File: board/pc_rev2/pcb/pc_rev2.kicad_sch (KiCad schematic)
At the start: 17 parts, among them J1 Conn_01x24, J2 Conn_01x24, J3 GND Pins, J4 Conn_Grove_Host, J5 Conn_Grove-Analog_Host, J6 Conn_Grove-Analog_Host, J7 Conn_01x05, U1 Tang_nano_9K, U2 AE-FT234X

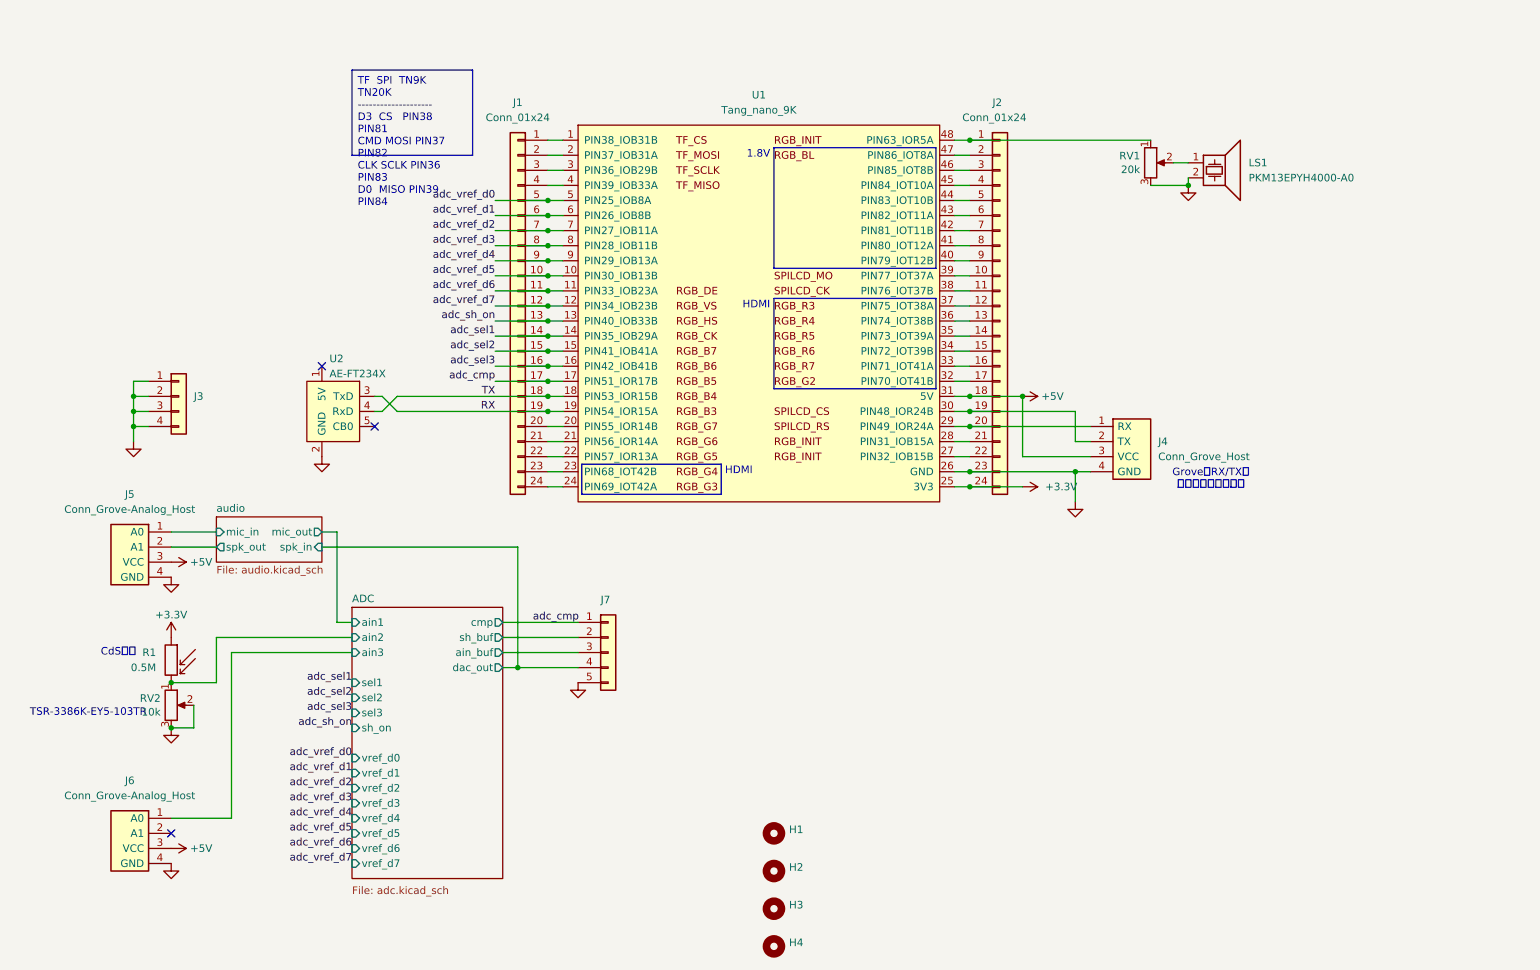
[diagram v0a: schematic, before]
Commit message: MSMP-IFを追加、スピーカ出力をOFFにする仕組みを追加（WIP）
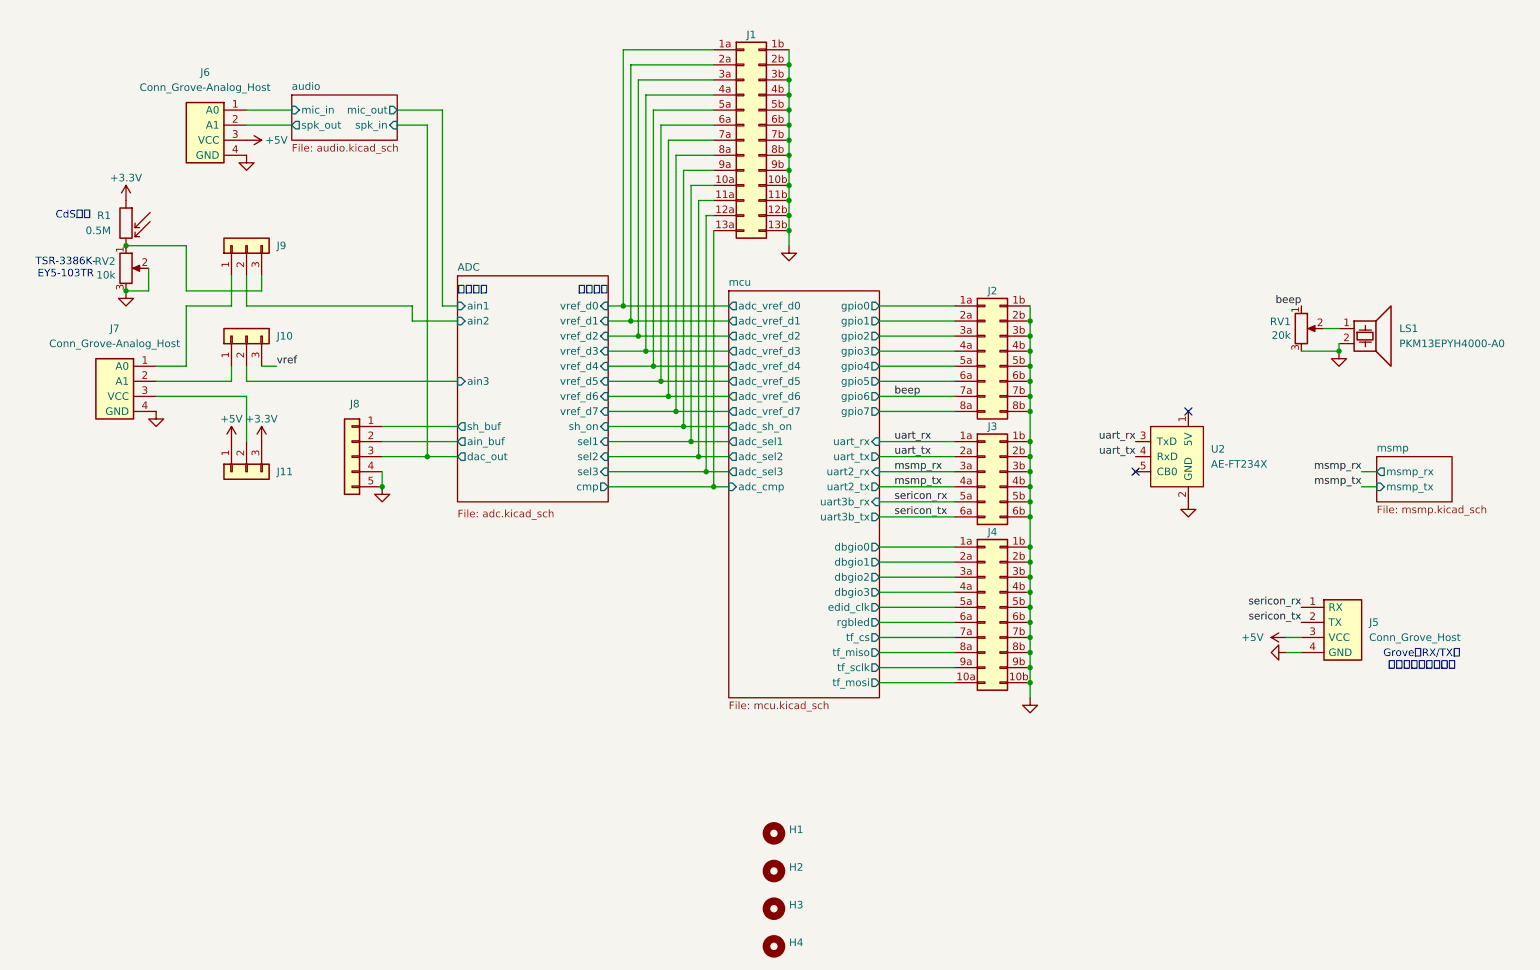
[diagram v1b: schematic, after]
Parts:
- removed J1, J2: Conn_01x24, Connector_PinHeader_2.54mm:PinHeader_1x24_P2.54mm_Vertical, symbol Connector_Generic:Conn_01x24
- removed J3: GND Pins, Connector_PinHeader_2.54mm:PinHeader_1x04_P2.54mm_Vertical, symbol Connector_Generic:Conn_01x04
- removed U1: Tang_nano_9K, uchan:DIP-48_Tang-Nano-9K, symbol uchan:Tang_nano_9K
- added J1: Conn_02x13_Odd_Even, symbol Connector_Generic:Conn_02x13_Row_Letter_Last
- added J10, J11, J9: Conn_01x03, Connector_PinHeader_2.54mm:PinHeader_1x03_P2.54mm_Vertical, symbol Connector_Generic:Conn_01x03
- added J2: Conn_02x08_Row_Letter_Last, symbol Connector_Generic:Conn_02x08_Row_Letter_Last
- added J3: Conn_02x06_Row_Letter_Last, symbol Connector_Generic:Conn_02x06_Row_Letter_Last
- added J4: Conn_02x10_Row_Letter_Last, symbol Connector_Generic:Conn_02x10_Row_Letter_Last
- renumbered J4 to J5, J5 to J6, J6 to J7, J7 to J8
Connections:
- net adc_cmp is gone; now on net ADC/sh_buf: J8.1 (Pin_1)
- net +3.3V: now also J11.3 (Pin_3)
- net +5V: now also J11.1 (Pin_1); no longer J7.3 (VCC)
- net ADC/ain2: now also J9.2 (Pin_2); no longer R1.2, RV2.1
- net ADC/ain3: now also J10.2 (Pin_2); no longer J7.1 (A0)
- net ADC/ain_buf: now also J8.2 (Pin_2); no longer J8.3 (Pin_3)
- net ADC/dac_out: now also J8.3 (Pin_3); no longer J8.4 (Pin_4)
- net ADC/sh_buf: no longer J8.2 (Pin_2)
- net GND: now also J8.4 (Pin_4), J1.10b (Pin_10b), J1.11b (Pin_11b), J1.12b (Pin_12b), J1.13b (Pin_13b), J1.1b (Pin_1b), J1.2b (Pin_2b), J1.3b (Pin_3b), J1.4b (Pin_4b), J1.5b (Pin_5b), J1.6b (Pin_6b), J1.7b (Pin_7b), J1.8b (Pin_8b), J1.9b (Pin_9b), J2.1b (Pin_1b), J2.2b (Pin_2b), J2.3b (Pin_3b), J2.4b (Pin_4b), J2.5b (Pin_5b), J2.6b (Pin_6b), J2.7b (Pin_7b), J2.8b (Pin_8b), J3.1b (Pin_1b), J3.2b (Pin_2b), J3.3b (Pin_3b), J3.4b (Pin_4b), J3.5b (Pin_5b), J3.6b (Pin_6b), J4.10b (Pin_10b), J4.1b (Pin_1b), J4.2b (Pin_2b), J4.3b (Pin_3b), J4.4b (Pin_4b), J4.5b (Pin_5b), J4.6b (Pin_6b), J4.7b (Pin_7b), J4.8b (Pin_8b), J4.9b (Pin_9b)
- net beep: now reaches RV1.1
- net beep: now also J2.7a (Pin_7a)
- net sericon_rx: now reaches J5.1 (RX)
- net sericon_rx: now also J3.5a (Pin_5a)
- net sericon_tx: now reaches J5.2 (TX)
- net sericon_tx: now also J3.6a (Pin_6a)
- net at J7.2 (A1): now also J10.1 (Pin_1)
- net RX renamed uart_rx
- net uart_rx: now also J3.1a (Pin_1a)
- net TX renamed uart_tx
- net uart_tx: now also J3.2a (Pin_2a)
- new net: J9.3 (Pin_3), R1.2, RV2.1
- new net: J11.2 (Pin_2), J7.3 (VCC)
- new net: J7.1 (A0), J9.1 (Pin_1)
- new net ADC/cmp: J1.13a (Pin_13a)
- new net ADC/sel1: J1.10a (Pin_10a)
- new net ADC/sel2: J1.11a (Pin_11a)
- new net ADC/sel3: J1.12a (Pin_12a)
- new net ADC/sh_on: J1.9a (Pin_9a)
- new net ADC/vref_d0: J1.1a (Pin_1a)
- new net ADC/vref_d1: J1.2a (Pin_2a)
- new net ADC/vref_d2: J1.3a (Pin_3a)
- new net ADC/vref_d3: J1.4a (Pin_4a)
- new net ADC/vref_d4: J1.5a (Pin_5a)
- new net ADC/vref_d5: J1.6a (Pin_6a)
- new net ADC/vref_d6: J1.7a (Pin_7a)
- new net ADC/vref_d7: J1.8a (Pin_8a)
- new net mcu/dbgio0: J4.1a (Pin_1a)
- new net mcu/dbgio1: J4.2a (Pin_2a)
- new net mcu/dbgio2: J4.3a (Pin_3a)
- new net mcu/dbgio3: J4.4a (Pin_4a)
- new net mcu/edid_clk: J4.5a (Pin_5a)
- new net mcu/gpio0: J2.1a (Pin_1a)
- new net mcu/gpio1: J2.2a (Pin_2a)
- new net mcu/gpio2: J2.3a (Pin_3a)
- new net mcu/gpio3: J2.4a (Pin_4a)
- new net mcu/gpio4: J2.5a (Pin_5a)
- new net mcu/gpio5: J2.6a (Pin_6a)
- new net mcu/gpio7: J2.8a (Pin_8a)
- new net mcu/rgbled: J4.6a (Pin_6a)
- new net mcu/tf_cs: J4.7a (Pin_7a)
- new net mcu/tf_miso: J4.8a (Pin_8a)
- new net mcu/tf_mosi: J4.10a (Pin_10a)
- new net mcu/tf_sclk: J4.9a (Pin_9a)
- new net msmp_rx: J3.3a (Pin_3a)
- new net msmp_tx: J3.4a (Pin_4a)
- new net vref: J10.3 (Pin_3)
- no-connect marks 3 -> 2
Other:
- added sheet mcu (mcu.kicad_sch)
- added sheet msmp (msmp.kicad_sch)
- note added: "TSR-3386K- EY5-103TR"
- note added: "アナログ"
- note added: "デジタル"
- note removed: "1.8V"
- note removed: "HDMI"
- note removed: "TSR-3386K-EY5-103TR"
- moved on the sheet: J5, J6, J7, J8, LS1, R1, RV1, RV2, U2

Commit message: ADCの8ch化＆スピーカーミュートの仕組み変更
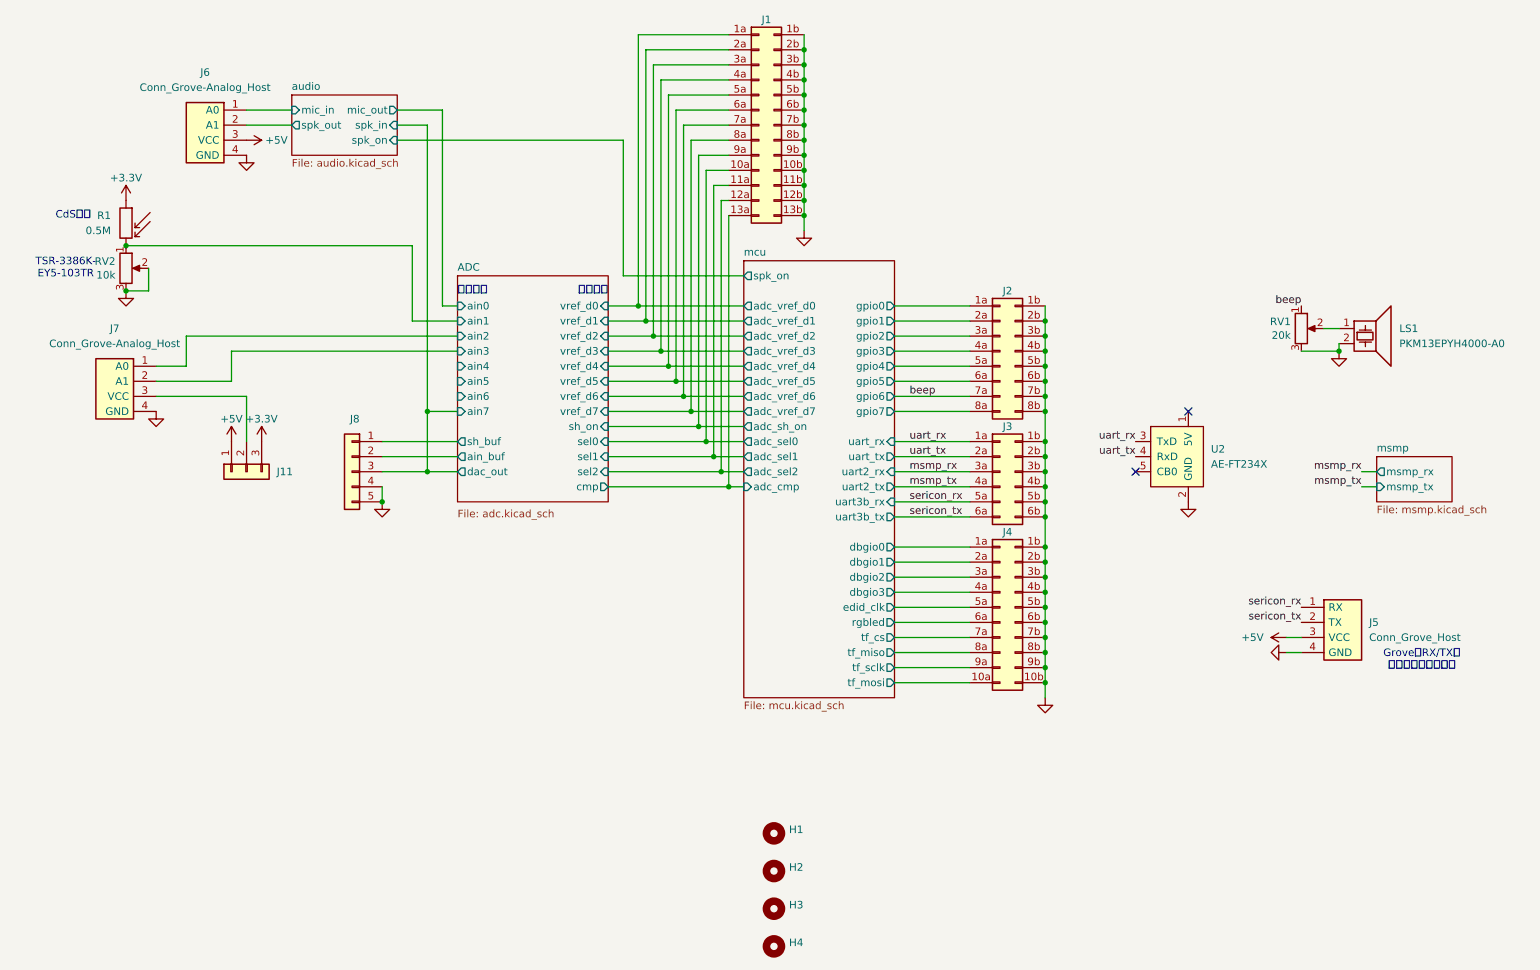
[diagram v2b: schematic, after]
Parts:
- removed J10, J9: Conn_01x03, Connector_PinHeader_2.54mm:PinHeader_1x03_P2.54mm_Vertical, symbol Connector_Generic:Conn_01x03
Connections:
- net ADC/sel3 is gone; now on net ADC/sel2: J1.12a (Pin_12a)
- net ADC/ain1: now also R1.2, RV2.1
- net ADC/ain2: now also J7.1 (A0)
- net ADC/ain3: now also J7.2 (A1)
- net ADC/sel1: now also J1.11a (Pin_11a); no longer J1.10a (Pin_10a)
- net ADC/sel2: no longer J1.11a (Pin_11a)
- net ADC/dac_out renamed ADC/ain7
- new net ADC/sel0: J1.10a (Pin_10a)
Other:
- sheet ADC ports: added ain0, ain4, ain5, ain6, ain7, sel0; removed sel3
- sheet audio ports: added spk_on; removed none
- sheet mcu ports: added adc_sel0, spk_on; removed adc_sel3
- moved on the sheet: J1, J2, J3, J4, J8

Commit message: 諸々改良＆基板デザイン（WIP）
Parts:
- removed J6: Conn_Grove-Analog_Host, uchan:Grove_1x04_P2mm_THT_Horizontal, symbol uchan:Conn_Grove-Analog_Host
- removed U2: AE-FT234X, uchan:AE-FT234X, symbol uchan:AE-FT234X
- added J14, J20: Conn_01x03, Connector_PinHeader_2.54mm:PinHeader_1x03_P2.54mm_Vertical, symbol Connector_Generic:Conn_01x03
- added J6, J7: Conn_01x03, Connector_JST:JST_XH_S2B-XH-A_1x02_P2.50mm_Horizontal, symbol Connector_Generic:Conn_01x02
- added J9: Conn_Grove-Analog_Host, uchan:Grove_1x04_P2mm_THT_Horizontal, symbol uchan:Conn_Grove-Analog_Host
- added U2: SKU2782, uchan:SKU2782, symbol uchan:SKU2782
- J1: footprint (none) -> Connector_PinHeader_2.54mm:PinHeader_2x14_P2.54mm_Vertical; symbol Connector_Generic:Conn_02x13_Row_Letter_Last -> Connector_Generic:Conn_02x14_Odd_Even
- J10: renamed from J8; footprint Connector_PinHeader_2.54mm:PinHeader_1x05_P2.54mm_Vertical -> Connector_PinHeader_2.54mm:PinHeader_1x03_P2.54mm_Vertical; symbol Connector_Generic:Conn_01x05 -> Connector_Generic:Conn_01x03
- J2: footprint (none) -> Connector_PinHeader_2.54mm:PinHeader_2x08_P2.54mm_Vertical; symbol Connector_Generic:Conn_02x08_Row_Letter_Last -> Connector_Generic:Conn_02x08_Odd_Even
- J3: footprint (none) -> Connector_PinHeader_2.54mm:PinHeader_2x06_P2.54mm_Vertical; symbol Connector_Generic:Conn_02x06_Row_Letter_Last -> Connector_Generic:Conn_02x06_Odd_Even
- J4: footprint (none) -> Connector_PinHeader_2.54mm:PinHeader_2x10_P2.54mm_Vertical; symbol Connector_Generic:Conn_02x10_Row_Letter_Last -> Connector_Generic:Conn_02x10_Odd_Even
- LS1: value PKM13EPYH4000-A0 -> 13mm; Manufacturer (none) -> Murata; Manufacturer PN (none) -> PKM13EPYH4000-A0
- R1: Manufacturer (none) -> Senba; Manufacturer PN (none) -> GL5516; Purpose (none) -> CdSセル。周辺の明るさを取得する
- RV1: footprint Potentiometer_SMD:Potentiometer_Bourns_TC33X_Vertical -> uchan:Potentiometer_Suntan_TSR-3386K_Vertical; Manufacturer (none) -> Suntan; Manufacturer PN (none) -> TSR-3386K-EY5-203TR
- RV2: Manufacturer (none) -> SUNTAN; Manufacturer PN (none) -> TSR-3386K-EY5-103TR
- renumbered J7 to J8
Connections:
- net ADC/ain7 is gone; now on net ADC/ain_buf: J10.3 (Pin_3)
- net +3.3V: now also J14.3 (Pin_3)
- net +5V: now also J14.1 (Pin_1)
- net ADC/ain4: now also J9.1 (A0)
- net ADC/ain5: now also J9.2 (A1)
- net ADC/ain_buf: no longer J10.2 (Pin_2)
- net ADC/cmp: now also J1.20 (Pin_20); no longer J1.13a (Pin_13a)
- net ADC/sel0: now also J1.22 (Pin_22); no longer J1.10a (Pin_10a)
- net ADC/sel1: now also J1.24 (Pin_24); no longer J1.11a (Pin_11a)
- net ADC/sel2: now also J1.26 (Pin_26); no longer J1.12a (Pin_12a)
- net ADC/sh_on: now also J1.18 (Pin_18); no longer J1.9a (Pin_9a)
- net ADC/vref_d0: now also J1.2 (Pin_2); no longer J1.1a (Pin_1a)
- net ADC/vref_d1: now also J1.4 (Pin_4); no longer J1.2a (Pin_2a)
- net ADC/vref_d2: now also J1.6 (Pin_6); no longer J1.3a (Pin_3a)
- net ADC/vref_d3: now also J1.8 (Pin_8); no longer J1.4a (Pin_4a)
- net ADC/vref_d4: now also J1.10 (Pin_10); no longer J1.5a (Pin_5a)
- net ADC/vref_d5: now also J1.12 (Pin_12); no longer J1.6a (Pin_6a)
- net ADC/vref_d6: now also J1.14 (Pin_14); no longer J1.7a (Pin_7a)
- net ADC/vref_d7: now also J1.16 (Pin_16); no longer J1.8a (Pin_8a)
- net GND: now also J1.1 (Pin_1), J1.11 (Pin_11), J1.13 (Pin_13), J1.15 (Pin_15), J1.17 (Pin_17), J1.19 (Pin_19), J1.21 (Pin_21), J1.23 (Pin_23), J1.25 (Pin_25), J1.27 (Pin_27), J1.3 (Pin_3), J1.5 (Pin_5), J1.7 (Pin_7), J1.9 (Pin_9), J2.1 (Pin_1), J2.11 (Pin_11), J2.13 (Pin_13), J2.15 (Pin_15), J2.3 (Pin_3), J2.5 (Pin_5), J2.7 (Pin_7), J2.9 (Pin_9), J3.10 (Pin_10), J3.12 (Pin_12), J3.2 (Pin_2), J3.4 (Pin_4), J3.6 (Pin_6), J3.8 (Pin_8), J4.1 (Pin_1), J4.11 (Pin_11), J4.13 (Pin_13), J4.15 (Pin_15), J4.17 (Pin_17), J4.19 (Pin_19), J4.3 (Pin_3), J4.5 (Pin_5), J4.7 (Pin_7), J4.9 (Pin_9), J20.1 (Pin_1), J20.2 (Pin_2), J20.3 (Pin_3), J6.2 (Pin_2), J7.2 (Pin_2), J9.4 (GND), U2.6 (GND); no longer J1.10b (Pin_10b), J1.11b (Pin_11b), J1.12b (Pin_12b), J1.13b (Pin_13b), J1.1b (Pin_1b), J1.2b (Pin_2b), J1.3b (Pin_3b), J1.4b (Pin_4b), J1.5b (Pin_5b), J1.6b (Pin_6b), J1.7b (Pin_7b), J1.8b (Pin_8b), J1.9b (Pin_9b), J10.4 (Pin_4), J10.5 (Pin_5), J2.1b (Pin_1b), J2.2b (Pin_2b), J2.3b (Pin_3b), J2.4b (Pin_4b), J2.5b (Pin_5b), J2.6b (Pin_6b), J2.7b (Pin_7b), J2.8b (Pin_8b), J3.1b (Pin_1b), J3.2b (Pin_2b), J3.3b (Pin_3b), J3.4b (Pin_4b), J3.5b (Pin_5b), J3.6b (Pin_6b), J4.10b (Pin_10b), J4.1b (Pin_1b), J4.2b (Pin_2b), J4.3b (Pin_3b), J4.4b (Pin_4b), J4.5b (Pin_5b), J4.6b (Pin_6b), J4.7b (Pin_7b), J4.8b (Pin_8b), J4.9b (Pin_9b)
- net audio/mic_in: now also J6.1 (Pin_1)
- net audio/spk_on: now also J1.28 (Pin_28)
- net audio/spk_out: now also J7.1 (Pin_1)
- net beep: now also J2.14 (Pin_14); no longer J2.7a (Pin_7a)
- net mcu/dbgio0: now also J4.2 (Pin_2); no longer J4.1a (Pin_1a)
- net mcu/dbgio1: now also J4.4 (Pin_4); no longer J4.2a (Pin_2a)
- net mcu/dbgio2: now also J4.6 (Pin_6); no longer J4.3a (Pin_3a)
- net mcu/gpio0: now also J2.2 (Pin_2); no longer J2.1a (Pin_1a)
- net mcu/gpio1: now also J2.4 (Pin_4); no longer J2.2a (Pin_2a)
- net mcu/gpio2: now also J2.6 (Pin_6); no longer J2.3a (Pin_3a)
- net mcu/gpio3: now also J2.8 (Pin_8); no longer J2.4a (Pin_4a)
- net mcu/gpio4: now also J2.10 (Pin_10); no longer J2.5a (Pin_5a)
- net mcu/gpio5: now also J2.12 (Pin_12); no longer J2.6a (Pin_6a)
- net mcu/gpio7: now also J2.16 (Pin_16); no longer J2.8a (Pin_8a)
- net mcu/rgbled: now also J4.12 (Pin_12); no longer J4.6a (Pin_6a)
- net mcu/tf_cs: now also J4.14 (Pin_14); no longer J4.7a (Pin_7a)
- net mcu/tf_miso: now also J4.16 (Pin_16); no longer J4.8a (Pin_8a)
- net mcu/tf_mosi: now also J4.20 (Pin_20); no longer J4.10a (Pin_10a)
- net mcu/tf_sclk: now also J4.18 (Pin_18); no longer J4.9a (Pin_9a)
- net msmp_rx: now also J3.5 (Pin_5); no longer J3.3a (Pin_3a)
- net msmp_tx: now also J3.7 (Pin_7); no longer J3.4a (Pin_4a)
- net sericon_rx: now also J3.9 (Pin_9); no longer J3.5a (Pin_5a)
- net sericon_tx: now also J3.11 (Pin_11); no longer J3.6a (Pin_6a)
- net uart_rx: now also J3.1 (Pin_1), U2.3 (TxD); no longer J3.1a (Pin_1a)
- net uart_tx: now also J3.3 (Pin_3), U2.2 (RxD); no longer J3.2a (Pin_2a)
- removed net mcu/dbgio3: J4.4a (Pin_4a)
- removed net mcu/edid_clk: J4.5a (Pin_5a)
- new net: J14.2 (Pin_2), J9.3 (VCC)
- new net ADC/dac_out: J10.2 (Pin_2)
- new net mcu/scl: J4.10 (Pin_10)
- new net mcu/sda: J4.8 (Pin_8)
- no-connect marks 2 -> 3
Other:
- sheet ADC ports: added none; removed ain6, ain7
- sheet mcu ports: added scl, sda; removed dbgio3, edid_clk
- note removed: "CdSセル"
- note removed: "TSR-3386K- EY5-103TR"
- moved on the sheet: J11, J2, J3, J4
